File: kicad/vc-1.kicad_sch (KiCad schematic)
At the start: 14 parts, among them J15 RESET SW, Q1 MJE180, U100 LM2903

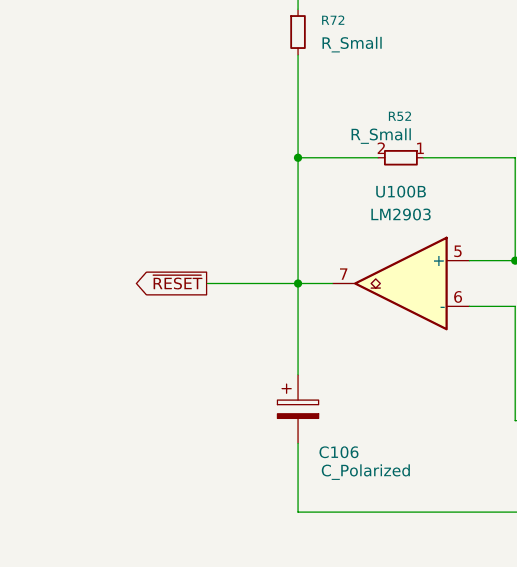
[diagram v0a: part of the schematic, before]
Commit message: Fixes to clocks,  keyboard controller stuff.
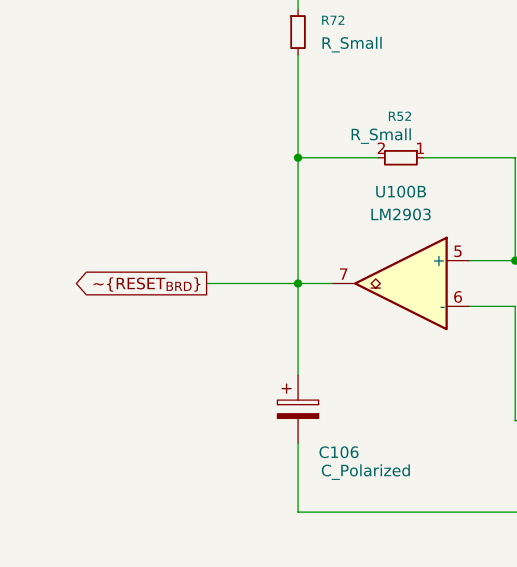
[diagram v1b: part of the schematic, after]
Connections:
- net ~{RESET} renamed ~{RESET_{BRD}}
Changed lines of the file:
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@@
 		)
 	)
-	(global_label "~{RESET}"
+	(global_label "~{RESET_{BRD}}"
 		(shape output)
 		(at 64.77 104.14 180)

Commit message: update kicad project
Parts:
- added U89: 74LS04, Package_DIP:DIP-14_W7.62mm, symbol 74xx:74LS04
- C106: seq_coord (none) -> L4
- D2: seq_coord (none) -> K1; seq_silkscreen (none) -> VR-1
- J15, R53: seq_coord (none) -> L1
- Q1: seq_coord (none) -> K1; seq_silkscreen B C E -> B C E
- R49, R50, R51, R52: seq_coord (none) -> L3
- R7: seq_coord (none) -> K2
- R72: seq_coord (none) -> L9
- R8, R9: seq_coord (none) -> K1
- U100: seq_coord (none) -> L2; seq_silkscreen (none) -> LM2903
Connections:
- net ~{RESET_{BRD}}: now also U89.1
- new net RESET_{BRD}: U89.2

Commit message: More updates
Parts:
- C106: value C_Polarized -> 47µF; seq_notes (none) -> Orange Electrolytic can,; seq_partno (none) -> Sprague 503D
- R49: value R_Small -> 6.49kΩ; seq_notes (none) -> Blue, Yellow, White, Brown, Brown (Blue body)
- R50, R72: value R_Small -> 1.1kΩ; seq_notes (none) -> Brown, Brown, Red, Gold
- R51: value R_Small -> 20kΩ; seq_notes (none) -> Red, Black, Black, Red, Gold (Red faded to orange)
- R52: value R_Small -> 200kΩ; seq_notes (none) -> Red, Black, Yellow, Gold
- R53: value ??Ω -> 300Ω; seq_notes (none) -> Orange, Black, Brown, Gold
- R8: value ??Ω -> 56Ω; seq_notes (none) -> Green, Blue, Black, Gold
- R9: value ??Ω -> 22Ω; seq_notes (none) -> Red, Red, Black, Gold
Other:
- moved on the sheet: D2, R7, U100C
